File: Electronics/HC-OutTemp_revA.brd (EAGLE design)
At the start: 80 x 80 mm, 38 parts, among them Q1 16MHz, SW1 SWITCH_SLIDE, U1 ATMEGA328-20P, U2 NRF24L01, U5 BCO35

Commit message: changed: PCB
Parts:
- removed BAT2: 1V5, 1_domaci:1XAA_BATTERY_HOLDER
- removed C2, C3: 22p, 1_domaci:C0805
- removed JP1, JP4, JP5, JP6: PINHD-3X1, 1_domaci:PINHD-3X1
- removed Q1: 16MHz, crystal:HC49/S
- removed R10, R2, R3, R7: 4K7, 1_domaci:R0805
- removed R4: 1M, 1_domaci:R0805
- removed U5: BCO35, 1_domaci:BCO35
- added U$9: CASE'120X80X40', 1_domaci:CASE-120X80X40
- added U3: TMP102, 1_domaci:TMP102
- BAT1: value 1V5 -> (none); device 1_domaci:1XAA_BATTERY_HOLDER -> 1_domaci:2XAA_BATTERY_HOLDER
- LED1: value green -> (none); device 1_domaci:LED0805 -> 1_domaci:LED3MM
- moved SW1 93.2 mm to (86.7, 23.1), turned to 90 degrees
- moved R1 86.5 mm to (88.0, 53.7), turned to 180 degrees
- moved JP2 85.9 mm to (86.7, 56.0), turned to 180 degrees
- moved U$7 84.7 mm to (18.4, 69.2)
- moved JP3 82.8 mm to (78.7, 56.0), turned to 0 degrees
- moved C4 77.9 mm to (83.7, 53.7), turned to 0 degrees
- moved U$5 69.5 mm to (101.0, 69.2)
- moved U$8 58.1 mm to (18.4, 10.8)
- moved C1 53.4 mm to (66.0, 53.7), turned to 180 degrees
- moved C5 48.6 mm to (66.5, 41.5), turned to 180 degrees
- moved C6 48.4 mm to (62.2, 41.5)
- moved U1 44.5 mm to (66.0, 47.6), turned to 180 degrees
- moved LED1 37.8 mm to (86.7, 50.0), flipped to the top, turned to 0 degrees
- moved BUT1 35.8 mm to (59.1, 57.0), turned to 0 degrees
- moved R6 30.9 mm to (59.7, 53.7)
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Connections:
- removed net DS18B20_1: JP4.2, R10.1, U1.13
- removed net DS18B20_2: JP1.2, R2.1, U1.14
- removed net DS18B20_3: JP5.2, R3.1, U1.15
- removed net DS18B20_4: JP6.2, R7.1, U1.16
- removed net N$11: LED1.1, R9.1
- removed net N$4: C2.2, Q1.2, R4.2, U1.9
- removed net N$8: BAT1.P, BAT2.P, SW1.2
- removed net V_BAT: SW1.3, U1.23, U5.IN
- new net N$10: U1.28, U3.SCL
- new net N$12: U1.26, U3.ALT
- new net N$3: LED1.A, R9.1
- new net N$9: U1.27, U3.SDA
- net +3V3: now also SW1.3, U3.VCC; no longer JP1.1, JP4.1, JP5.1, JP6.1, R10.2, R2.2, R3.2, R7.2, U5.OUT
- net BUT: now also U1.11; no longer U1.4
- net CE_R: now also U1.13; no longer U1.24
- net CS_R: now also U1.14; no longer U1.25
- net GND: now also LED1.K, U3.GND; no longer BAT2.N, C2.1, C3.1, JP1.3, JP4.3, JP5.3, JP6.3, LED1.2, U5.GND
- net LED: now also U1.25; no longer U1.5
- net N$1: now also BAT1.P, SW1.2; no longer C3.2, Q1.1, R4.1, U1.10
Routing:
- net +3V3: track 0.00 -> 136.7 mm
- net GND: track 0.00 -> 132.3 mm
- net SCK: track 0.00 -> 22.8 mm
- net CE_R: track 0.00 -> 20.1 mm
- net MOSI: track 0.00 -> 17.8 mm
- net MISO: track 0.00 -> 16.9 mm
- net CS_R: track 0.00 -> 15.9 mm
- net N$12: track 0.00 -> 12.4 mm
- net N$7: track 0.00 -> 11.1 mm
- net N$3: track 0.00 -> 10.1 mm
- net N$1: track 0.00 -> 9.67 mm
- net N$9: track 0.00 -> 9.49 mm
- net N$2: track 0.00 -> 8.11 mm
- net N$10: track 0.00 -> 6.82 mm
- net TX: track 0.00 -> 4.57 mm
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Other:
- board size 80 x 80 mm -> 89.4 x 65.3 mm

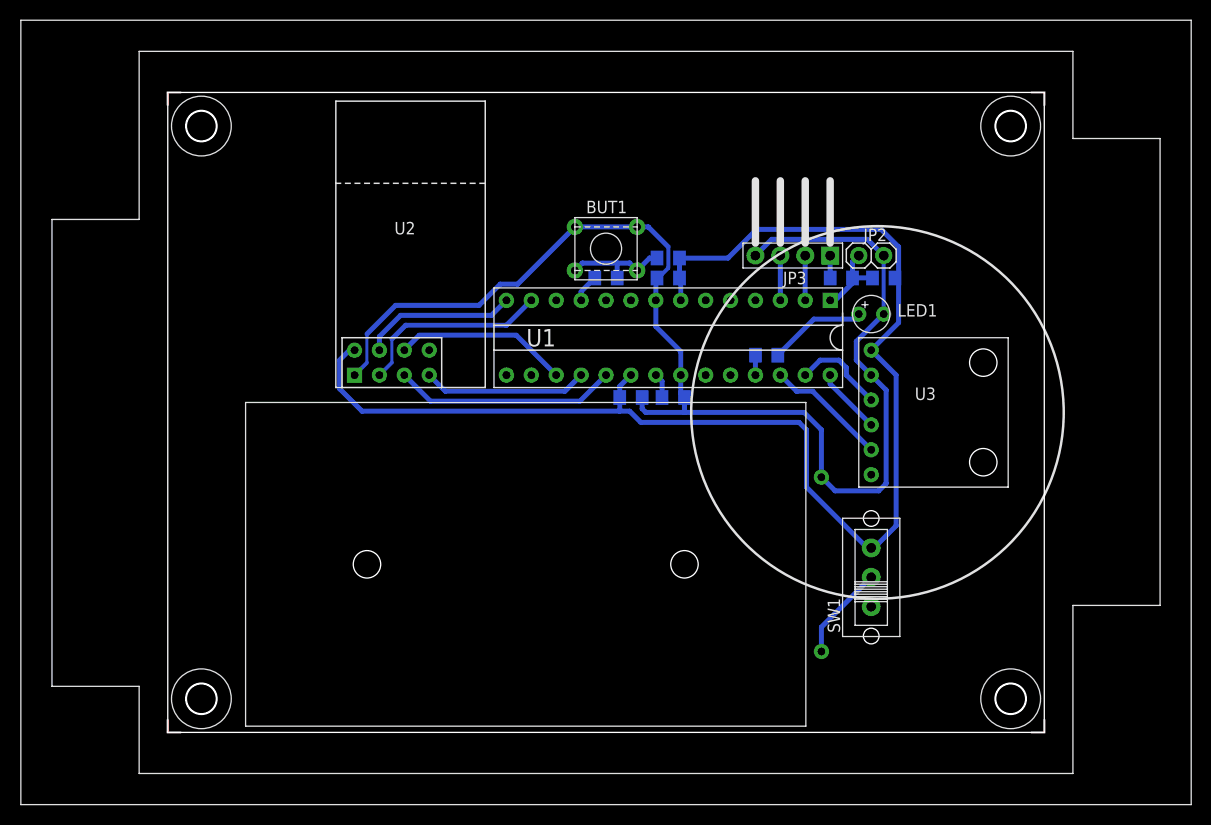
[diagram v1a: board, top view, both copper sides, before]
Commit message: changed: MCU package to SMD
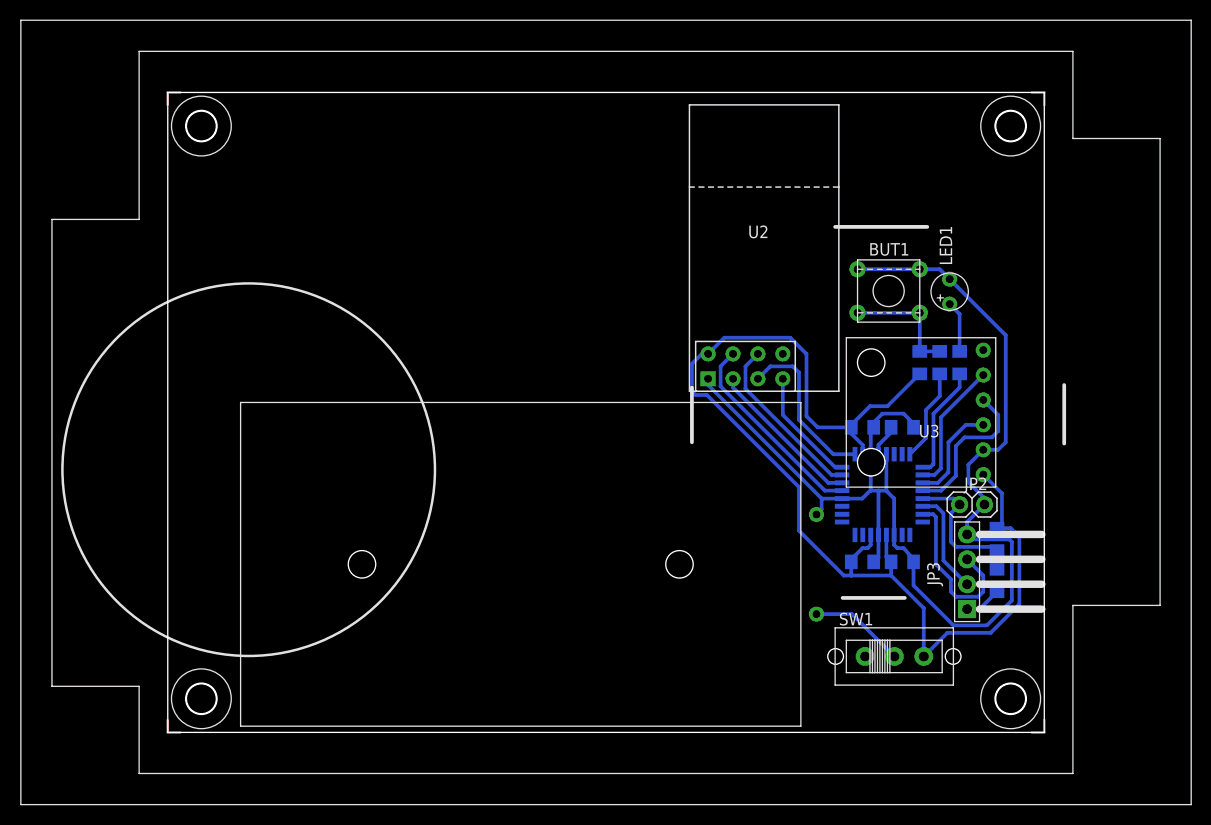
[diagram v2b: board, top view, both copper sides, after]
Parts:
- added C2: 100n, 1_domaci:C0805
- U1: value ATMEGA328-20P -> ATMEGA328P-AU; device 1_domaci:DIL28-3 -> 1_domaci:QFP80P900X900X120-32N
- moved JP3 36.8 mm to (96.5, 23.7), turned to 270 degrees
- moved U2 36.1 mm to (75.2, 44.7)
- moved R6 35.1 mm to (93.7, 45.1), turned to 90 degrees
- moved C1 35.1 mm to (85.9, 24.8), turned to 0 degrees
- moved C4 34.7 mm to (99.6, 22.9), turned to 270 degrees
- moved BUT1 29.2 mm to (87.9, 52.7)
- moved R1 29.1 mm to (99.6, 27.1), turned to 90 degrees
- moved R5 27.8 mm to (91.7, 45.1), turned to 270 degrees
- moved JP2 27.4 mm to (97.0, 30.6)
- moved U1 27.1 mm to (87.9, 31.6), flipped to the bottom, turned to 90 degrees
- moved C6 23.8 mm to (85.9, 38.5)
- moved C5 23.6 mm to (89.9, 38.5)
- moved R9 19.7 mm to (95.8, 45.1), turned to 270 degrees
- moved LED1 8.32 mm to (94.7, 52.3), turned to 90 degrees
- moved SW1 8.32 mm to (89.0, 15.1), turned to 0 degrees
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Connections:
- net +3V3: now also C2.2, U1.18, U1.4, U1.6; no longer U1.20, U1.7
- net BUT: now also U1.24; no longer U1.11
- net CE_R: now also U1.14; no longer U1.13
- net CS_R: now also U1.13; no longer U1.14
- net GND: now also C2.1, U1.12, U1.19, U1.21, U1.3, U1.5; no longer U1.22, U1.8
- net MISO: now also U1.16; no longer U1.18
- net MOSI: now also U1.15; no longer U1.17
- net N$2: now also U1.29; no longer U1.1
- net N$5: now also U1.20; no longer U1.21
- net RX: now also U1.30; no longer U1.2
- net SCK: now also U1.17; no longer U1.19
- net TX: now also U1.31; no longer U1.3
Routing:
- net +3V3: track 136.7 -> 118.0 mm
- net TX: track 4.57 -> 17.4 mm
- net LED: track 2.03 -> 11.5 mm
- net N$10: track 6.82 -> 15.8 mm
- net N$2: track 8.11 -> 15.2 mm
- net BUT: track 2.86 -> 9.47 mm
- net RX: track 4.57 -> 10.6 mm
- net GND: track 132.3 -> 126.2 mm
- net SCK: track 22.8 -> 17.0 mm
- net MISO: track 16.9 -> 11.9 mm
- net N$3: track 10.1 -> 5.25 mm
- net CS_R: track 15.9 -> 20.6 mm
- net CE_R: track 20.1 -> 16.0 mm
- net N$6: track 2.29 -> 3.78 mm
- net N$7: track 11.1 -> 12.3 mm
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
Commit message: modified: PCB
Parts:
- added R2: 0R, 1_domaci:R0805
- BAT1: value (none) -> 2xAA
- R9: value 1K -> ?K
- moved R1 3.64 mm to (100.3, 30.6)
- moved C4 3.51 mm to (100.3, 26.3)
- moved SW1 0.72 mm to (88.5, 15.6)
- moved JP3 0.57 mm to (97.0, 23.5)
- moved C1 0.51 mm to (85.9, 24.3)
- moved C2 0.51 mm to (89.9, 24.3)
- moved C5 0.51 mm to (89.9, 39.0)
- moved C6 0.51 mm to (85.9, 39.0)
- moved R5 0.38 mm to (91.3, 45.1)
- moved R6 0.38 mm to (93.3, 45.1)
- moved R9 0.38 mm to (95.4, 45.1)
- moved JP2 0.13 mm to (96.9, 30.6)
- moved U3 0.13 mm to (91.9, 40.0)
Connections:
- new net N$8: JP3.2, R2.2
- net RX: now also R2.1; no longer JP3.2
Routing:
- net GND: track 126.2 -> 133.9 mm
- net TX: track 17.4 -> 11.4 mm
- net N$6: track 3.78 -> 8.62 mm
- net RX: track 10.6 -> 6.63 mm
- net N$8: track 0.00 -> 3.88 mm
- net N$2: track 15.2 -> 11.7 mm
- net +3V3: track 118.0 -> 115.8 mm
- net N$10: track 15.8 -> 17.2 mm
- net SCK: track 17.0 -> 18.1 mm
- net N$1: track 9.74 -> 9.02 mm

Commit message: modified: PCB
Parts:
- R9: value ?K -> 4k7
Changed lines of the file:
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@@
 <setting verticaltext="up"/>
 </settings>
-<grid distance="0.005" unitdist="inch" unit="mm" style="lines" multiple="1" display="yes" altdistance="0.00125" altunitdist="inch" altunit="inch"/>
+<grid distance="0.005" unitdist="inch" unit="inch" style="lines" multiple="1" display="yes" altdistance="0.00125" altunitdist="inch" altunit="inch"/>
 <layers>
 <layer number="1" name="Top" color="4" fill="1" visible="yes" active="yes"/>
@@
 <layer number="18" name="Vias" color="2" fill="1" visible="yes" active="yes"/>
 <layer number="19" name="Unrouted" color="6" fill="1" visible="yes" active="yes"/>
-<layer number="20" name="Dimension" color="15" fill="1" visible="no" active="yes"/>
+<layer number="20" name="Dimension" color="15" fill="1" visible="yes" active="yes"/>
 <layer number="21" name="tPlace" color="7" fill="1" visible="yes" active="yes"/>
-<layer number="22" name="bPlace" color="7" fill="1" visible="no" active="yes"/>
+<layer number="22" name="bPlace" color="7" fill="1" visible="yes" active="yes"/>
 <layer number="23" name="tOrigins" color="15" fill="1" visible="yes" active="yes"/>
 <layer number="24" name="bOrigins" color="15" fill="1" visible="yes" active="yes"/>
@@
 <board>
 <plain>
-<circle x="23.241" y="34.163" radius="19.00026875" width="0.254" layer="21"/>
+<circle x="87.376" y="40.005" radius="19.00026875" width="0.254" layer="21"/>
 <wire x1="14.986" y1="72.644" x2="14.986" y2="7.366" width="0.0254" layer="20"/>
 <wire x1="14.986" y1="7.366" x2="104.394" y2="7.366" width="0.0254" layer="20"/>
@@
 <dimension x1="104.394" y1="72.644" x2="14.986" y2="72.644" x3="59.69" y3="74.041" textsize="1.778" layer="20"/>
 <dimension x1="14.986" y1="72.644" x2="14.986" y2="7.366" x3="13.462" y3="40.005" textsize="1.778" layer="20"/>
-<wire x1="83.058" y1="58.928" x2="92.456" y2="58.928" width="0.381" layer="21"/>
-<wire x1="83.82" y1="21.082" x2="90.17" y2="21.082" width="0.381" layer="21"/>
-<wire x1="106.426" y1="36.83" x2="106.426" y2="42.799" width="0.381" layer="21"/>
-<wire x1="68.453" y1="42.545" x2="68.453" y2="36.957" width="0.381" layer="21"/>
 <circle x="67.183" y="24.511" radius="0.8" width="1.3" layer="116"/>
 <circle x="34.798" y="24.511" radius="0.8" width="1.3" layer="116"/>
@@
 <element name="U$7" library="1_domaci" package="HOLE" value="HOLE" x="18.415" y="69.215" smashed="yes" rot="R90"/>
 <element name="U$8" library="1_domaci" package="HOLE" value="HOLE" x="18.415" y="10.795" smashed="yes" rot="R90"/>
-<element name="R9" library="1_domaci" package="R0805" value="?K" x="95.377" y="45.085" smashed="yes" rot="MR270">
+<element name="R9" library="1_domaci" package="R0805" value="4k7" x="95.377" y="45.085" smashed="yes" rot="MR270">
 <attribute name="NAME" x="96.012" y="45.974" size="1.27" layer="26" rot="MR270"/>
 <attribute name="VALUE" x="95.885" y="45.974" size="1.27" layer="28" rot="MR270"/>
